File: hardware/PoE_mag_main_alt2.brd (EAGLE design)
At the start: 165.1 x 115.6 mm, 121 parts, among them IC1 LD1117S33TR, IC10 PCA9517A, IC2 DS1338, IC3 74LVC1T45SOT23-HAND, IC4 ATMEGA1284, IC5 MCP2200, IC6 TSR 1-2450, IC7 74LVC1T45SOT23-HAND, IC8 74LVC1T45SOT23-HAND, IC9 74LVC1T45SOT23-HAND, Q1 BSS138, Q3 BUK98150-55A, X1 PWR, X2 JTAG, X3 USB, X4 CONN-SMATHD, X5 UFL, X6 MICRO-SD-SOCKETHIROSE-DM3D, X7 RJ45, X8 RJ11, X9 22-23-2021, Y1 32k768, Y2 16MHz, Y3 12MHz

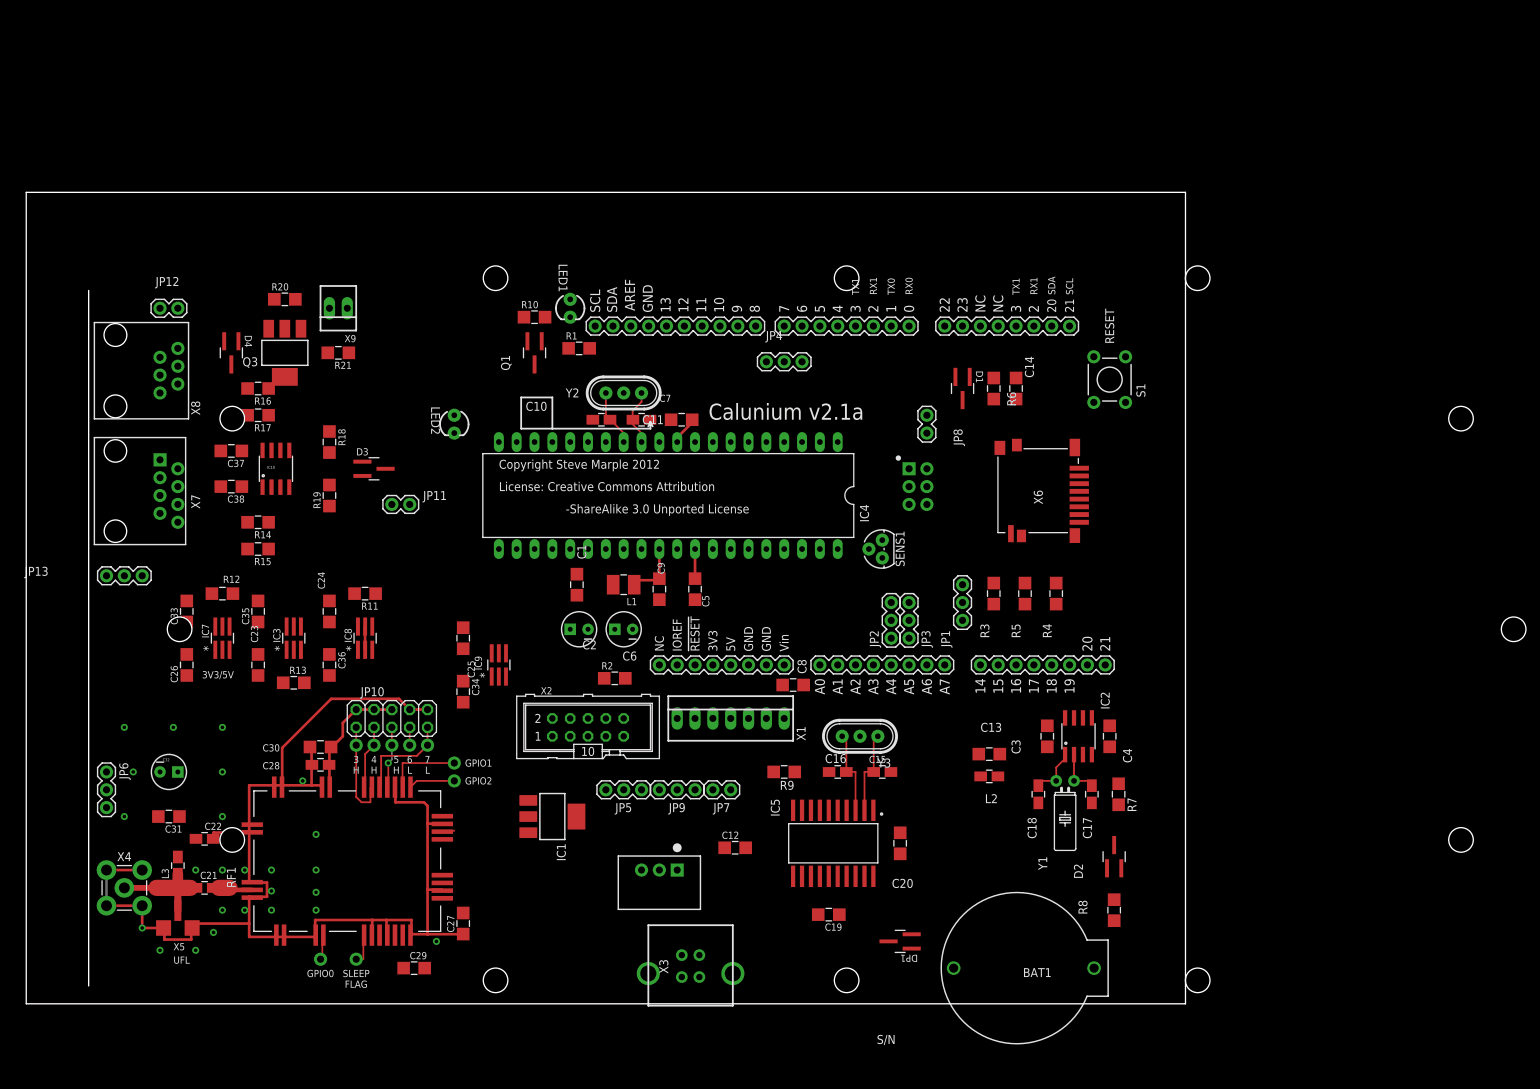
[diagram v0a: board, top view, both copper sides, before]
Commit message: Update enclosure outline
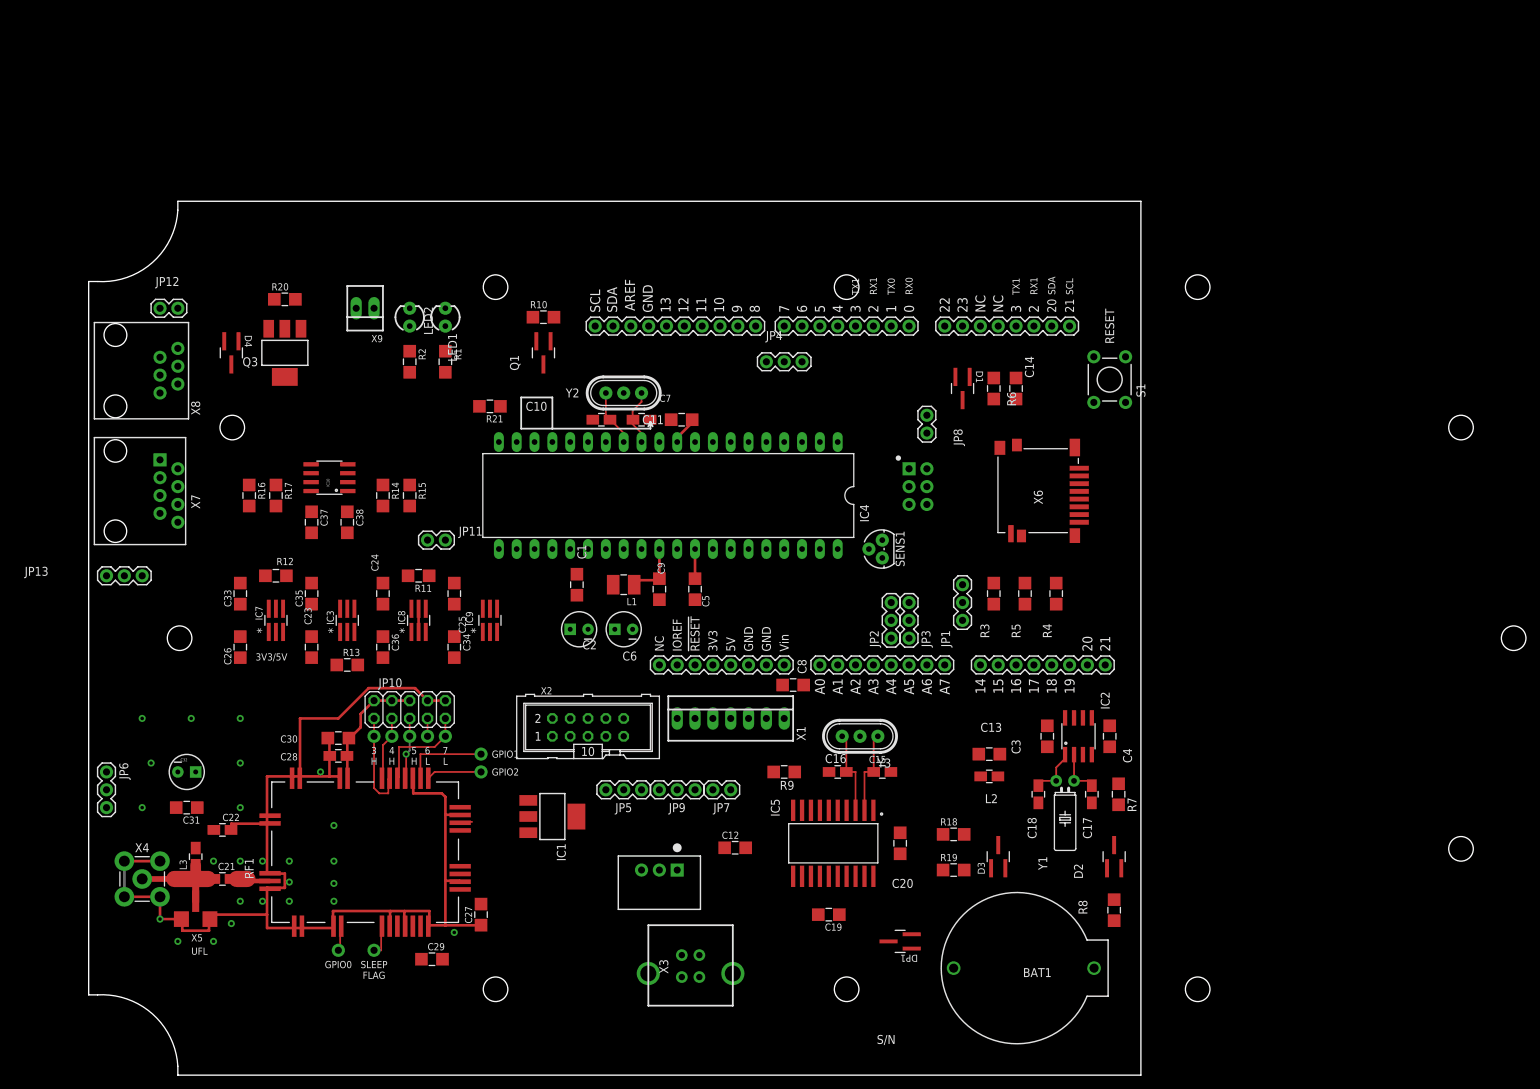
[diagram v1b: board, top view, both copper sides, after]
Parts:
- BOX1: value BOXFIBOX-PC-M-95-G -> BOXPOE-MAG-150-150; device fibox:FIBOX-PC-M-95-G -> fibox:FIBOX-PC-M-95-G-POE-MAG
- moved R18 105.0 mm to (123.2, 21.6), turned to 0 degrees
- moved D3 104.7 mm to (129.5, 18.4), turned to 90 degrees
- moved R19 103.7 mm to (123.2, 16.5), turned to 0 degrees
- moved R2 53.7 mm to (45.7, 88.9), turned to 270 degrees
- moved R15 22.9 mm to (45.7, 69.8), turned to 270 degrees
- moved R21 22.9 mm to (57.1, 82.5)
- moved R1 19.1 mm to (50.8, 88.9), turned to 270 degrees
- moved R14 18.2 mm to (41.9, 69.8), turned to 270 degrees
- moved LED1 17.8 mm to (50.8, 95.2), turned to 90 degrees
- moved C38 17.3 mm to (36.8, 66.0), turned to 270 degrees
- moved LED2 16.5 mm to (45.7, 95.2), turned to 90 degrees
- moved R16 15.3 mm to (22.9, 69.8), turned to 270 degrees
- moved C37 15.3 mm to (31.8, 66.0), turned to 270 degrees
- moved R17 11.7 mm to (26.7, 69.8), turned to 270 degrees
- moved IC8 8.03 mm to (47.0, 52.1)
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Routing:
- net GND: track 194.0 -> 195.9 mm
- net GPIO1: track 10.8 -> 12.1 mm
- net GPIO2: track 6.61 -> 7.88 mm
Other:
- board size 165.1 x 115.6 mm -> 149.9 x 124.5 mm

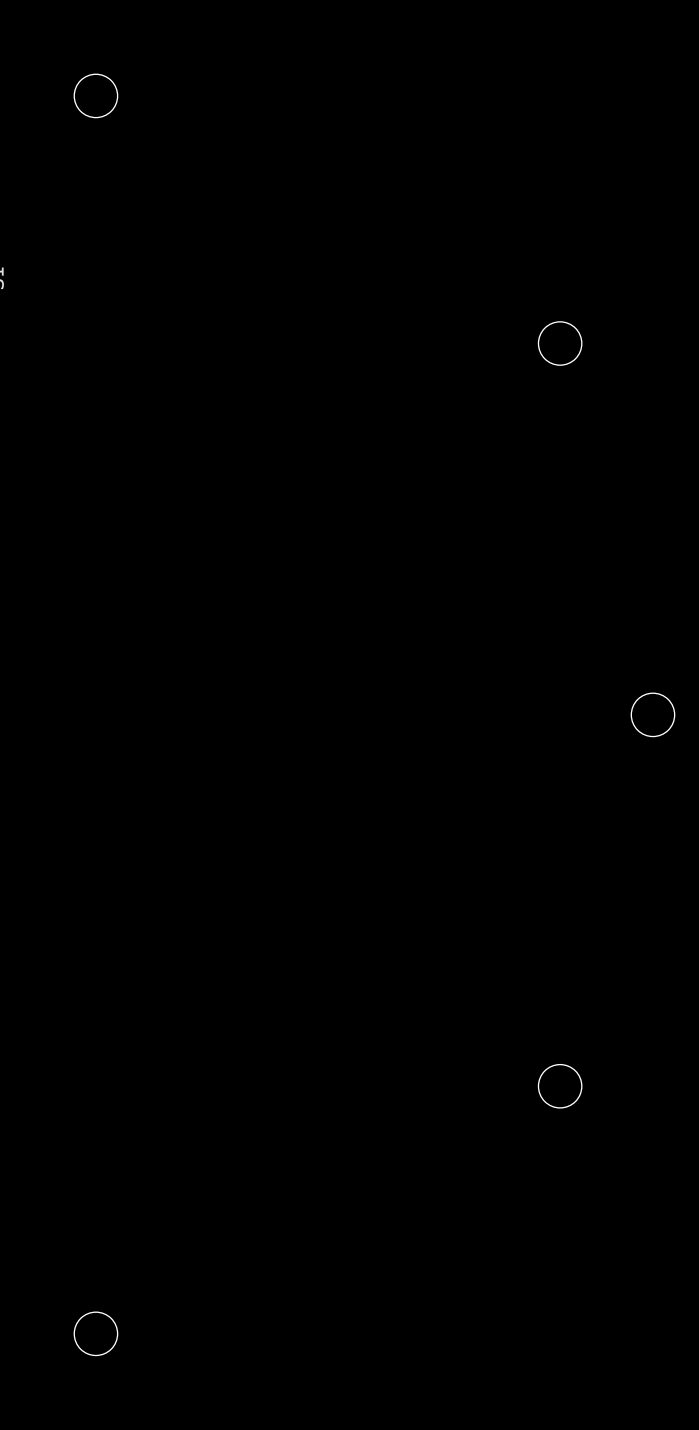
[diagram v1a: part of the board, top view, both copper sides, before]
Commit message: Update enclosure restrictions
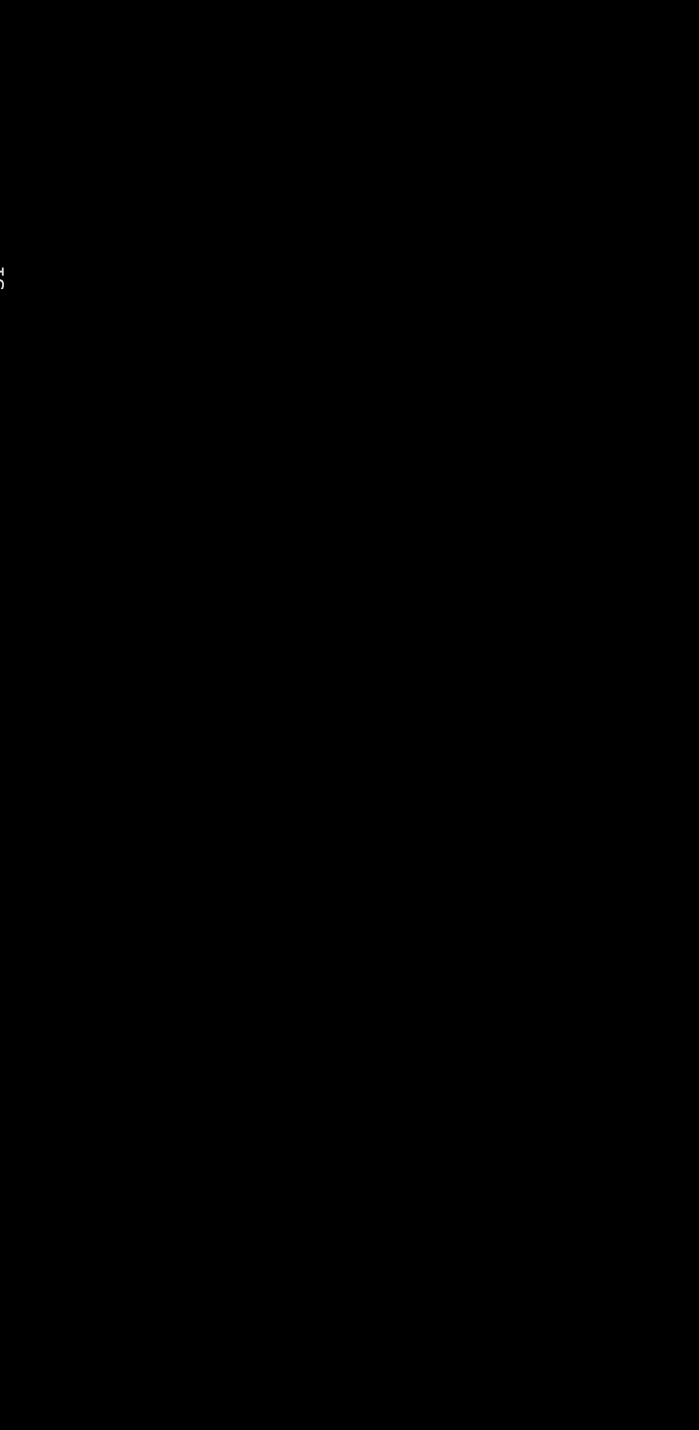
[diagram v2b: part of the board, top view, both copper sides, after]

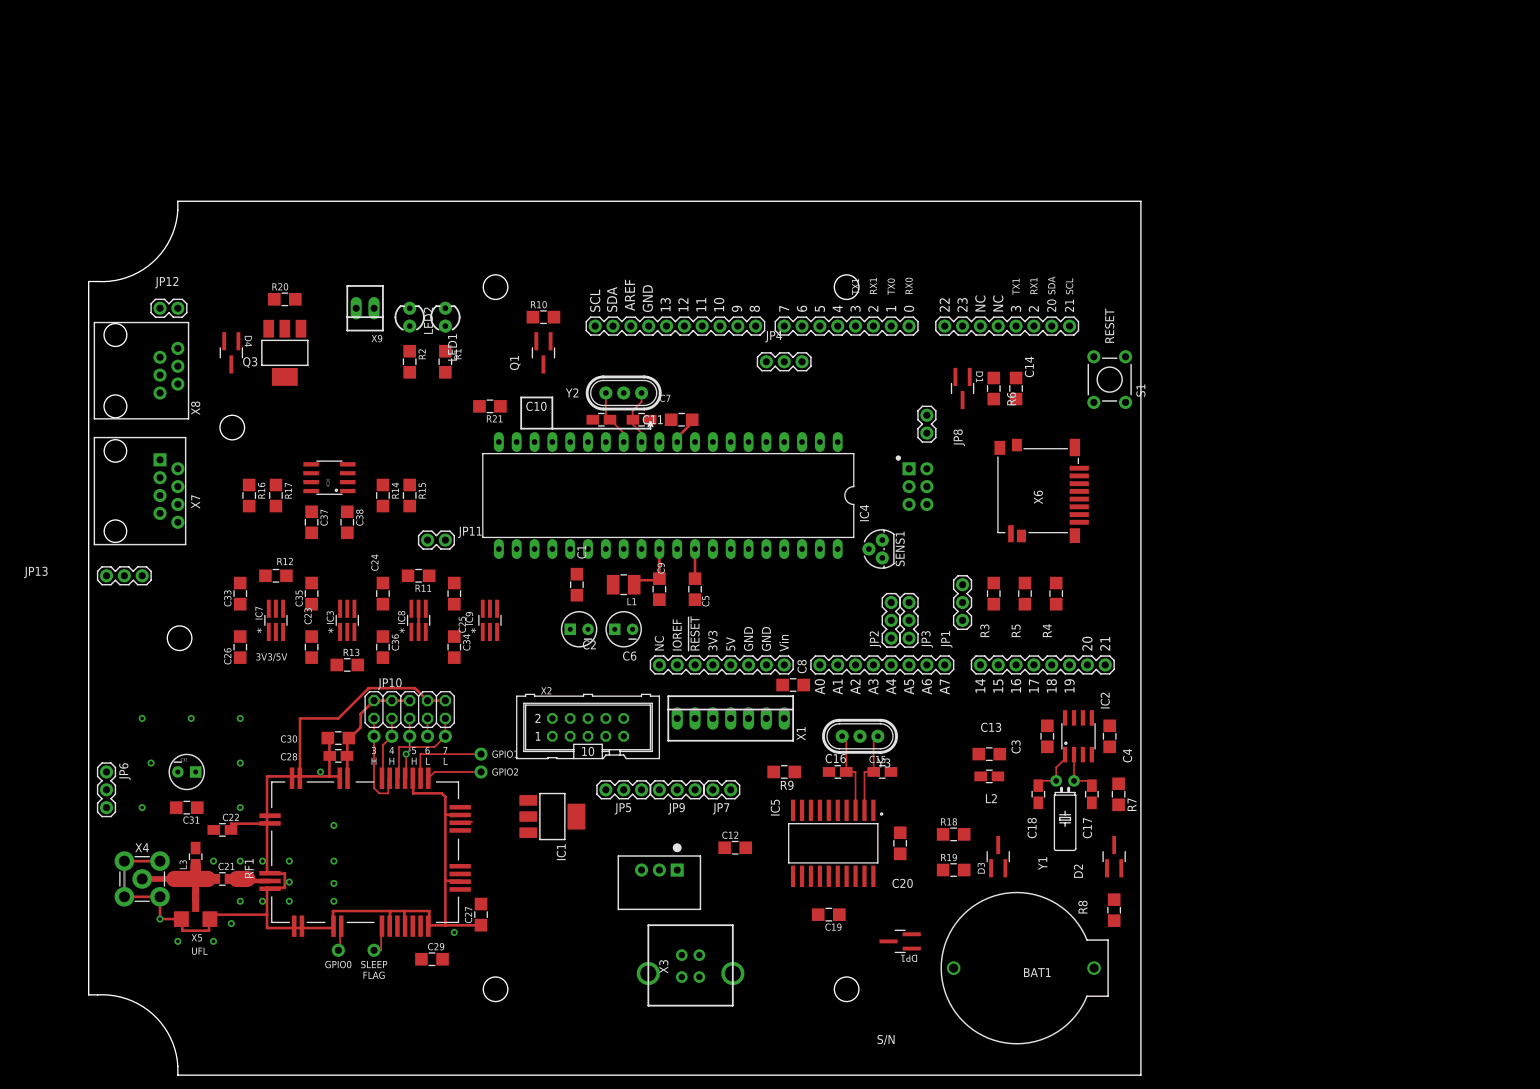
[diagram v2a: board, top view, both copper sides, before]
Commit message: Fix silkscreen text
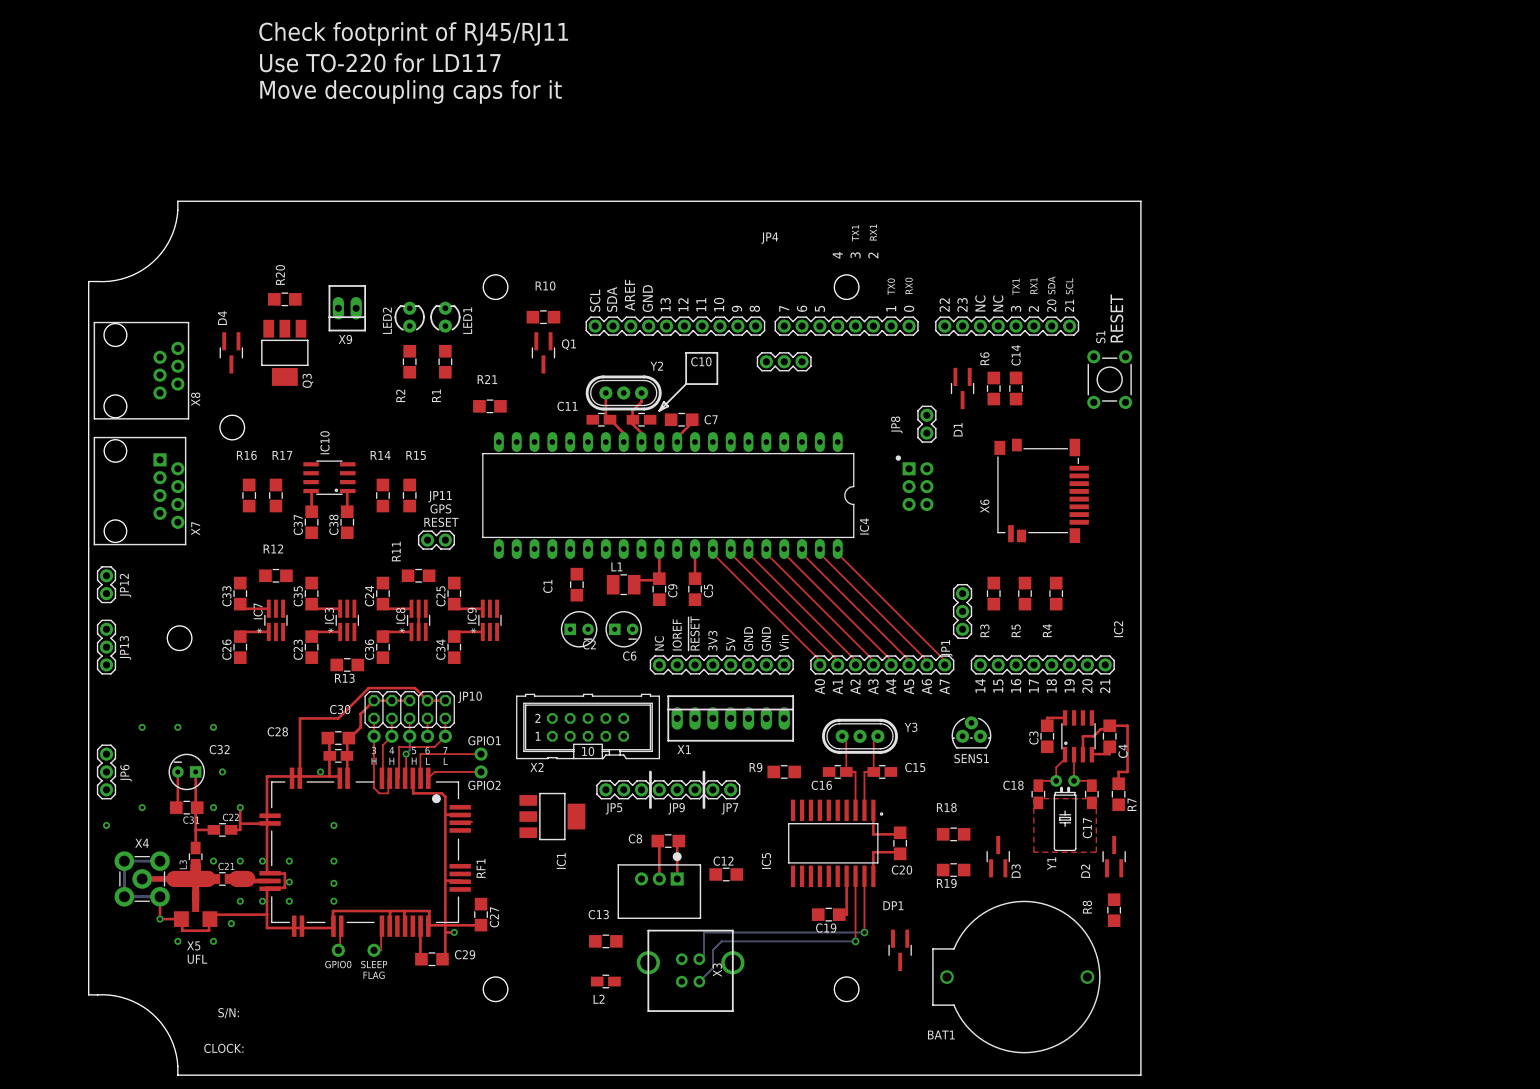
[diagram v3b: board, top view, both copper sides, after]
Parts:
- removed JP2: SDA/A4, SparkFun:1X03
- removed JP3: SCL/A5, SparkFun:1X03
- JP4: value PPS 7/6 -> PPS
- moved L2 61.9 mm to (73.7, 0.64), turned to 180 degrees
- moved C13 60.8 mm to (73.7, 6.35), turned to 0 degrees
- moved JP12 41.3 mm to (2.54, 55.9), turned to 90 degrees
- moved SENS1 29.5 mm to (125.7, 35.6), turned to 0 degrees
- moved C8 28.5 mm to (82.5, 20.6), turned to 180 degrees
- moved BAT1 19.1 mm to (142.2, 1.27), turned to 180 degrees
- moved JP13 7.62 mm to (2.54, 50.8), turned to 270 degrees
- moved C12 4.02 mm to (90.8, 15.9)
- moved JP6 2.54 mm to (2.54, 33.0)
- moved X3 2.54 mm to (85.7, 3.81), turned to 180 degrees
- moved X9 2.54 mm to (36.8, 96.5)
- moved IC6 1.27 mm to (81.3, 15.2)
- moved DP1 1.27 mm to (115.6, 5.08), turned to 270 degrees
- moved JP1 1.27 mm to (124.5, 55.9)
- turned C26 to 270 degrees
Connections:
- net N$16 renamed VBUS
- removed net A4/SDA: JP2.2, U$1.A4/SDA
- removed net A5/SCL: JP3.2, U$1.A5/SCL
- net 20(SDA): no longer JP2.3
- net 21(SCL): no longer JP3.3
- net A4: now also U$1.A4/SDA; no longer JP2.1
- net A5: now also U$1.A5/SCL; no longer JP3.1
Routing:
- net USB_D-: track 0.00 -> 35.4 mm, vias 0 -> 1
- net USB_D+: track 0.00 -> 35.3 mm, vias 0 -> 1
- net VCC: track 4.86 -> 37.9 mm
- net GND: track 195.9 -> 226.2 mm, vias 25 -> 26
- net +3V3: track 19.0 -> 49.2 mm
- net A5: track 0.00 -> 22.8 mm
- net A3: track 0.00 -> 22.8 mm
- net A1: track 0.00 -> 22.8 mm
- net A7: track 0.00 -> 22.8 mm
- net A6: track 0.00 -> 22.8 mm
- net A4: track 0.00 -> 22.8 mm
- net A2: track 0.00 -> 22.8 mm
- net A0: track 0.00 -> 22.8 mm
- net N$11: track 0.00 -> 20.5 mm
- net V_ANT: track 0.43 -> 13.5 mm
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- added copper zone on layer 1, net GND
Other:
- board text added: "3V3/VIN"
- board text added: "7/6"
- board text added: "CLOCK:"
- board text added: "Check footprint of RJ45/RJ11"
- board text added: "FAN"
- board text added: "GPS RESET"
- board text added: "POWER"
- board text added: "S/N:"
- board text added: "STATUS"
- board text added: "Use TO-220 for LD117 Move decoupling caps for it"
- board text removed: "+3V3"
- board text removed: "-ShareAlike 3.0 Unported License"
- board text removed: ">DRAWING_NAME"
- board text removed: ">PLOT_DATE_TIME"
- board text removed: "Arduino NV08C GPS Shield v1.0"
- board text removed: "Calunium v2.1a"
- board text removed: "Copyright Steve Marple 2012"
- board text removed: "License: Creative Commons Attribution"
- board text removed: "S/N"
- board text removed: "Steve Marple Lancaster University"
- board text removed: "VIN"
- board text removed: "calunium@stevemarple.co.uk"
- board text removed: "https://github.com/stevemarple/Calunium"
